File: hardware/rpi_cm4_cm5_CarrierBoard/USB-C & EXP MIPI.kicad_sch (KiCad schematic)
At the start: 17 parts, among them J16 12401598E4#2A, J17 5051102291, U23 AP22913W6-7

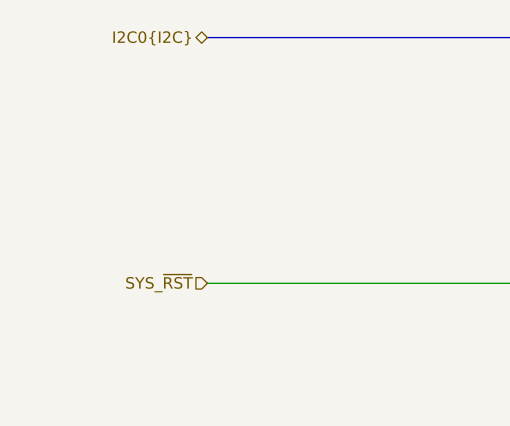
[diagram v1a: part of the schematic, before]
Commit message: Added power input protection & filter Added dedicated QWIIC connector on RPI CMx I2C6 bus Adjusted power table and PinMux Updated schematics accordingly
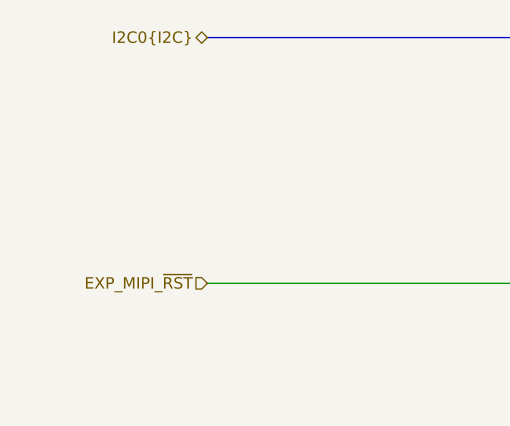
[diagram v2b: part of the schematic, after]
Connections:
- net SYS_~{RST} renamed EXP_MIPI_~{RST}
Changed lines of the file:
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@@
 		)
 	)
-	(hierarchical_label "SYS_~{RST}"
+	(hierarchical_label "EXP_MIPI_~{RST}"
 		(shape input)
 		(at 80.645 151.765 180)

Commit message: Update watchdog timer circuit to add external watchdog timer IC to be fed by PIC Adjust reset scheme in power supply sheet accordingly Adjust PinMux, regen BOM and PDF schematics (preliminary) Start preliminary component placement in the PCB
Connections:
- net USB_OTG.OTG_ID: now also D20.1; no longer D20.2 (A)
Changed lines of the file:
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@@
 	)
 	(no_connect
+		(at 191.135 54.61)
+	)
+	(no_connect
 		(at 248.285 31.115)
 	)
@@
 		(at 248.285 59.055)
 	)
-	(no_connect
-		(at 191.135 54.61)
-	)
 	(bus_entry
 		(at 143.51 94.615)
@@
 	(symbol
 		(lib_id "KicadCompDb:ESD Diodes/ESD_DIODE_00002")
-		(at 191.135 54.61 0)
-		(mirror y)
+		(at 188.595 54.61 0)
 		(unit 1)
 		(exclude_from_sim no)
@@
 		(dnp no)
 		(property "Reference" "D20"
-			(at 186.817 57.023 0)
+			(at 192.913 57.023 0)
 			(effects
 				(font
@@
 		)
 		(property "Value" "D1213A-02SOL-7"
-			(at 186.69 57.1499 0)
+			(at 193.04 57.1499 0)
 			(effects
 				(font
@@
 		)
 		(property "Footprint" "footprint:SOT-23-3"
-			(at 190.627 76.708 0)
+			(at 189.103 76.708 0)
 			(effects
 				(font
@@
 		)
 		(property "Datasheet" "https://www.diodes.com/assets/Datasheets/D1213A_02SOL.pdf"
-			(at 191.135 54.61 0)
+			(at 188.595 54.61 0)
 			(effects
 				(font
@@
 		)
 		(property "Description" "TVS DIODE 3.3VWM 10VC SOT233"
-			(at 189.357 64.516 0)
+			(at 190.373 64.516 0)
 			(effects
 				(font
@@
 		)
 		(property "V(r)" "3.3V"
-			(at 186.69 59.6899 0)
+			(at 193.04 59.6899 0)
 			(effects
 				(font
@@
 		)
 		(property "V(cl)" "10V"
-			(at 190.881 68.834 0)
+			(at 188.849 68.834 0)
 			(effects
 				(font
@@
 		)
 		(property "V(br)" "6V"
-			(at 191.135 70.866 0)
+			(at 188.595 70.866 0)
 			(effects
 				(font
@@
 		)
 		(property "I(pp)" "1A"
-			(at 191.135 54.61 0)
+			(at 188.595 54.61 0)
 			(effects
 				(font
@@
 		)
 		(property "Power" "NA"
-			(at 191.135 54.61 0)
+			(at 188.595 54.61 0)
 			(effects
 				(font
@@
 		)
 		(property "Capacitance" "0.85pF"
-			(at 191.135 54.61 0)
+			(at 188.595 54.61 0)
 			(effects
 				(font
@@
 		)
 		(property "Operating Temperature" "-55°C ~ 125°C"
-			(at 190.373 78.994 0)
+			(at 189.357 78.994 0)
 			(effects
 				(font
@@
 		)
 		(property "Package" "SOT-23-3"
-			(at 191.135 54.61 0)
+			(at 188.595 54.61 0)
 			(effects
 				(font
@@
 		)
 		(property "Manufacturer" "Diodes Incorporated"
-			(at 190.881 72.898 0)
+			(at 188.849 72.898 0)
 			(effects
 				(font
@@
 		)
 		(property "Manufacturer Part Number" "D1213A-02SOL-7"
-			(at 190.881 62.484 0)
+			(at 188.849 62.484 0)
 			(effects
 				(font
@@
 		)
 		(property "Distributor" "DigiKey"
-			(at 191.135 60.452 0)
+			(at 188.595 60.452 0)
 			(effects
 				(font
@@
 		)
 		(property "Distributor Part Number" "D1213A-02SOL-7DICT-ND"
-			(at 190.373 66.802 0)
+			(at 189.357 66.802 0)
 			(effects
 				(font
@@
 		)
 		(property "Type" "ESD TVS DUAL CA SMT"
-			(at 191.135 54.61 0)
+			(at 188.595 54.61 0)
 			(show_name yes)
 			(effects
@@
 		)
 		(property "Dimensions" "2.90mm x 2.40mm"
-			(at 191.135 54.61 0)
+			(at 188.595 54.61 0)
 			(show_name yes)
 			(effects

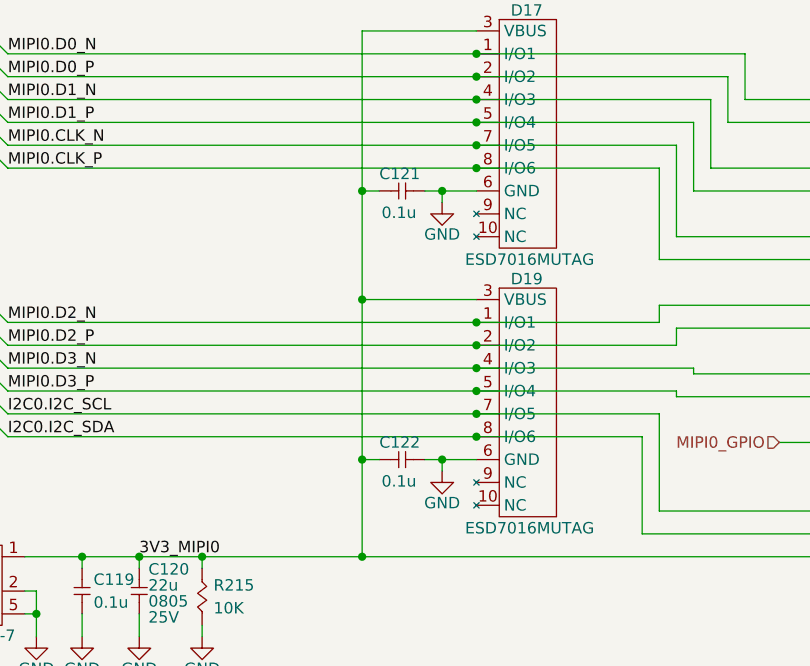
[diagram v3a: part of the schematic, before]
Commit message: Update schematics based on PCB preliminary placement Add preliminary design rules to PCB
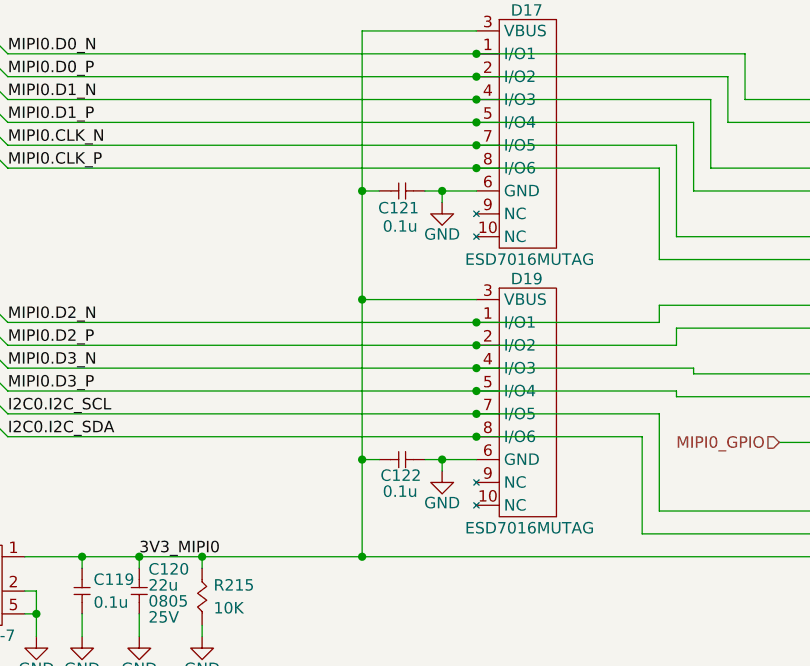
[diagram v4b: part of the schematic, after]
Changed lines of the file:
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@@
 		(dnp no)
 		(property "Reference" "C121"
-			(at 187.325 102.87 0)
+			(at 187.198 106.68 0)
 			(effects
 				(font
@@
 		)
 		(property "Value" "0.1u"
-			(at 187.579 107.188 0)
+			(at 187.706 108.712 0)
 			(effects
 				(font
@@
 		(dnp no)
 		(property "Reference" "C122"
-			(at 187.325 132.715 0)
+			(at 187.452 136.398 0)
 			(effects
 				(font
@@
 		)
 		(property "Value" "0.1u"
-			(at 187.579 137.033 0)
-			(effects
-				(font
+			(at 187.706 138.176 0)
+			(effects
+				(font

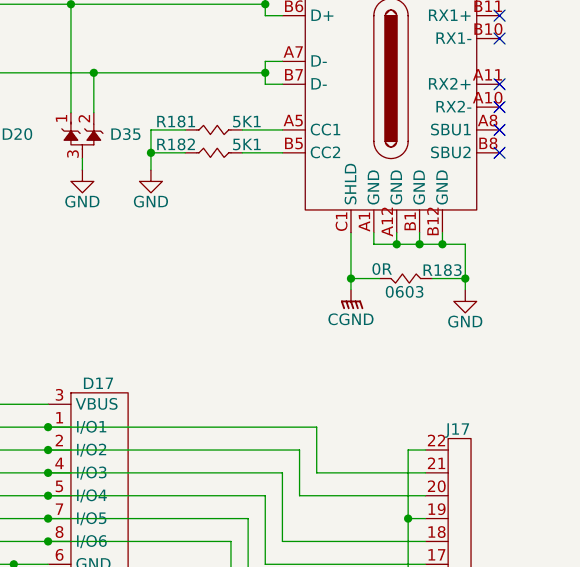
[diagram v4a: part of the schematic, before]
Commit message: Update PCB design rules for outer layers differential pairs Update preliminary component placement Update schematics based on PCB placement & remove duplicata / unnecessary components Update design notes and power table
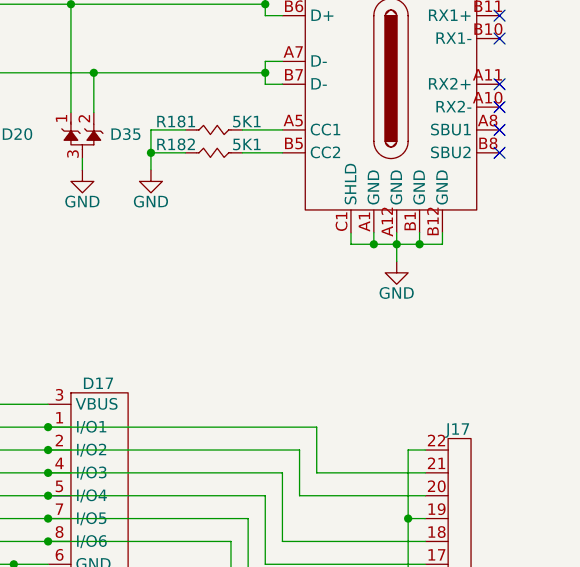
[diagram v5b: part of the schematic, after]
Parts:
- removed R183: 0R, footprint:RES_0603, symbol KicadCompDb:Resistors/RES_SMT_00021
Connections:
- net CGND is gone; now on net GND: J16.C1 (SHLD)

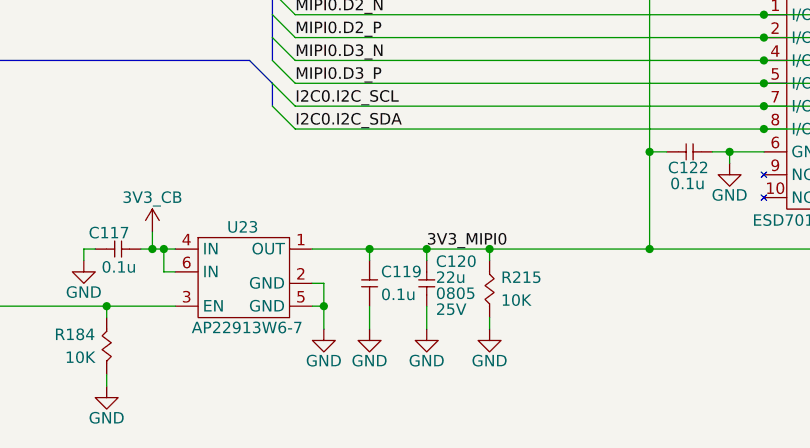
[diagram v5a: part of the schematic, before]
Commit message: Document stackup Few changes to schematic based on preliminary PCB placement Update PinMux based on preliminary PCB placement and component positions
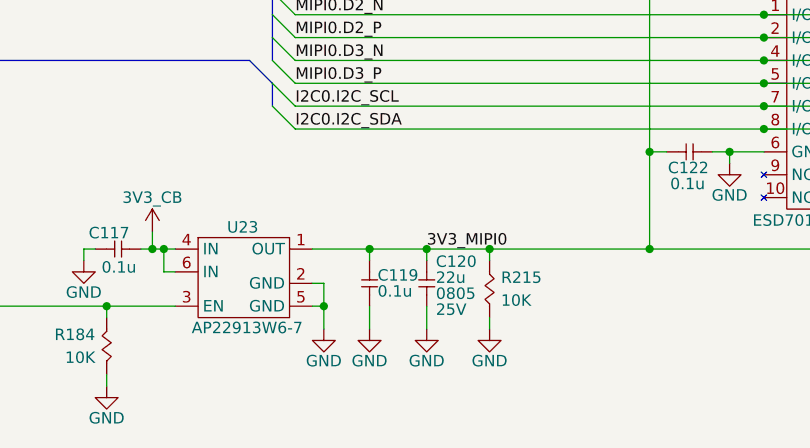
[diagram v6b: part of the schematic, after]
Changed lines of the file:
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@@
 	(title_block
 		(title "RPI CMx Carrier")
-		(date "2025-12-07")
+		(date "2026-01-22")
 		(rev "2.00-0A")
 		(comment 1 "Jean-Francois Bilodeau")
@@
 		(dnp no)
 		(property "Reference" "C119"
-			(at 155.575 147.955 90)
+			(at 155.194 148.336 90)
 			(effects
 				(font
@@
 		)
 		(property "Value" "0.1u"
-			(at 155.575 150.495 90)
+			(at 155.194 150.114 90)
 			(effects
 				(font
